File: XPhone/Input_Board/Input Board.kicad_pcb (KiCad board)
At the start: 2 copper layers, 100 x 100 mm, 94 parts, among them J1 AUDIO, J10 ENV, J11 PULSE, J12 PULSE, J13 Power In, J14 Power Out, J2 AUDIO, J3 ENV, J4 ENV, J5 PULSE, J6 PULSE, J7 AUDIO, J8 AUDIO, J9 ENV, Q1 BC847CW, Q2 BC847CW, Q3 BC847CW, Q4 BC847CW, Q5 BC847CW, Q6 BC847CW, Q7 BC847CW, Q8 BC847CW, U1 LM833, U2 78L05, U3 TL084, U4 74HC14, U5 LM833

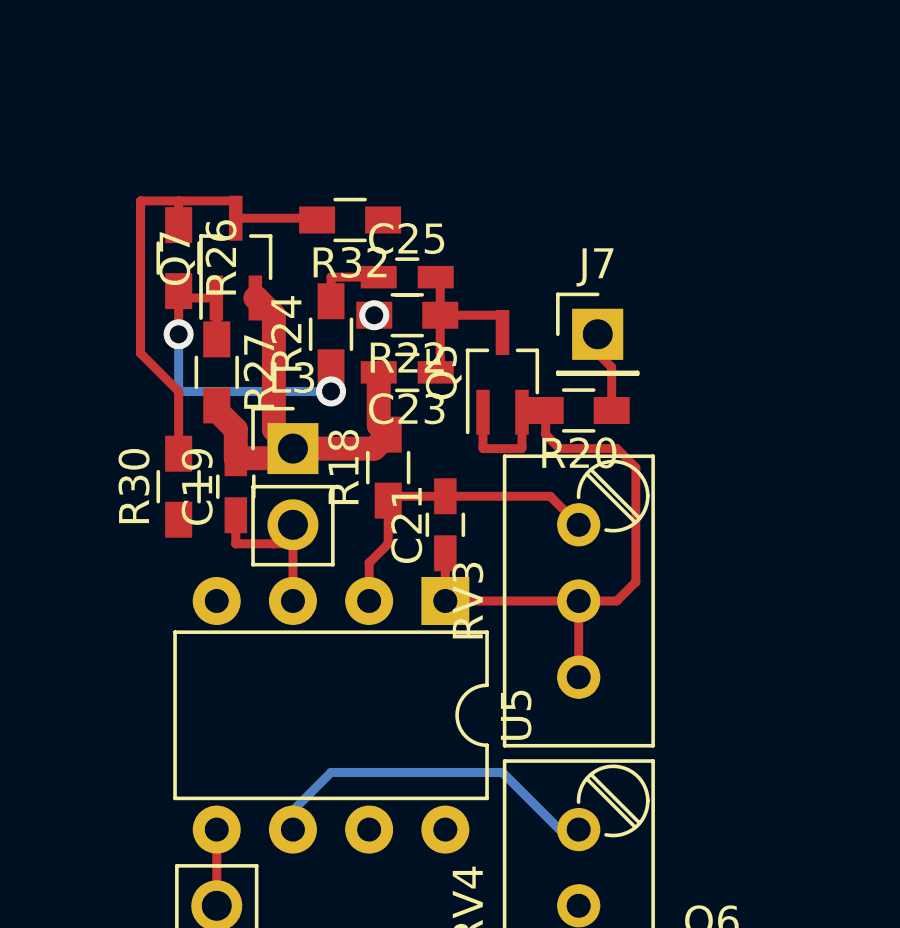
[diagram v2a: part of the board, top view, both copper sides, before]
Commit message: XPhone/Input_Board touching-up first layout of amplifier circuit
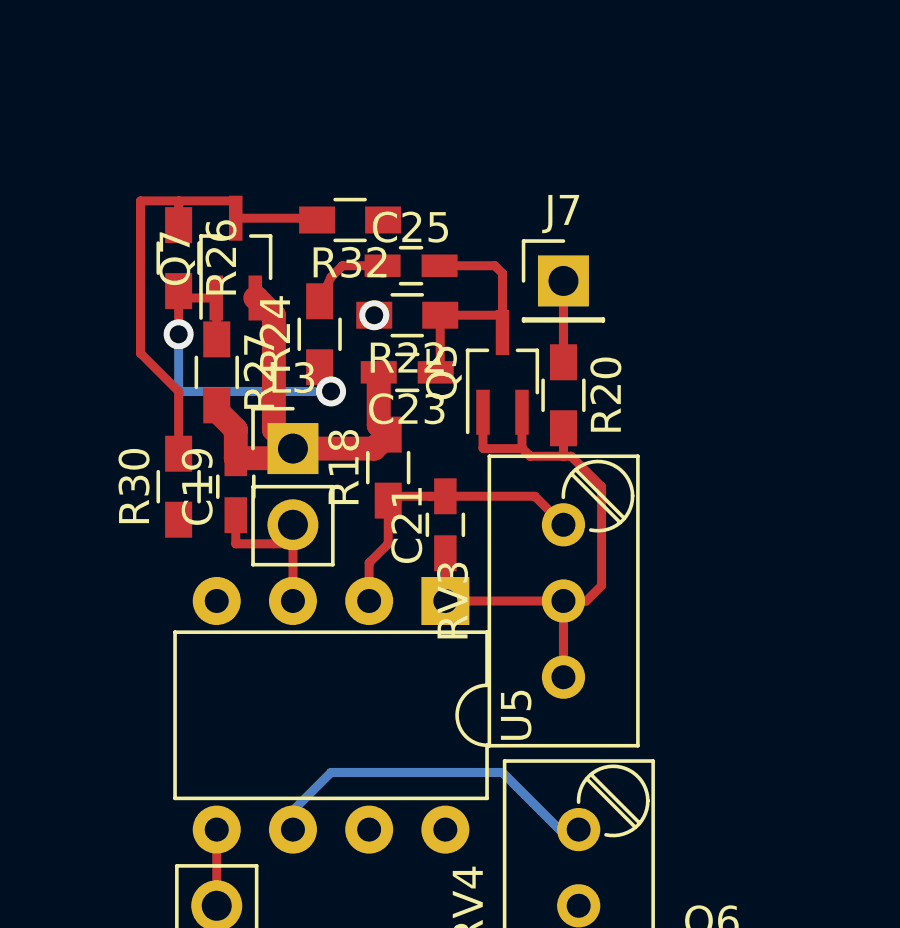
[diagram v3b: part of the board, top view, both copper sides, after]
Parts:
- moved J7 2.11 mm to (97.3, 45.2)
- moved R20 0.72 mm to (97.3, 49.0), turned to 270 degrees
- moved RV3 0.51 mm to (97.3, 53.3)
- moved C25 0.40 mm to (92.2, 44.7)
- moved R24 0.38 mm to (89.2, 47.0)
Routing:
- net Net-(C23-Pad1): track 6.03 -> 8.88 mm
- net Net-(C21-Pad1): track 23.3 -> 20.7 mm
- net Net-(C25-Pad1): track 2.40 -> 3.02 mm
- net Net-(C21-Pad2): track 10.4 -> 9.90 mm
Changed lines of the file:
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@@
   (general
     (links 173)
-    (no_connects 144)
+    (no_connects 145)
     (area 10.719999 10.719999 110.870001 110.870001)
     (thickness 1.6)
@@
   )
   (module Pin_Headers:Pin_Header_Straight_1x01_Pitch2.54mm (layer F.Cu)
-    (at 98.425 46.99)
+    (at 97.282 45.212)
     (descr "Through hole straight pin header, 1x01, 2.54mm pitch, single row")
     (tags "Through hole pin header THT 1x01 2.54mm single row")
@@
   )
   (module Potentiometers:Potentiometer_Trimmer_Bourns_3296W (layer F.Cu)
-    (at 97.79 53.34 90)
+    (at 97.282 53.34 90)
     (descr "Spindle Trimmer Potentiometer, Bourns 3296W, https://www.bourns.com/pdfs/3296.pdf")
     (tags "Spindle Trimmer Potentiometer   Bourns 3296W")
@@
   )
   (module Resistors_SMD:R_0603_HandSoldering (layer F.Cu)
-    (at 89.535 46.99 90)
+    (at 89.154 46.99 90)
     (descr "Resistor SMD 0603, hand soldering")
     (tags "resistor 0603")
@@
   )
   (module Resistors_SMD:R_0603_HandSoldering (layer F.Cu)
-    (at 97.79 49.53 180)
+    (at 97.282 49.022 270)
     (descr "Resistor SMD 0603, hand soldering")
     (tags "resistor 0603")
     (attr smd)
-    (fp_text reference R20 (at 0 -1.45 180) (layer F.SilkS)
+    (fp_text reference R20 (at 0 -1.45 270) (layer F.SilkS)
       (effects (font (size 1 1) (thickness 0.15)))
     )
-    (fp_text value 10k (at 0 1.55 180) (layer F.Fab)
+    (fp_text value 10k (at 0 1.55 270) (layer F.Fab)
       (effects (font (size 1 1) (thickness 0.15)))
     )
-    (fp_text user %R (at 0 0 180) (layer F.Fab)
+    (fp_text user %R (at 0 0 270) (layer F.Fab)
       (effects (font (size 0.5 0.5) (thickness 0.075)))
     )
@@
     (fp_line (start 1.95 0.7) (end 1.95 -0.7) (layer F.CrtYd) (width 0.05))
     (fp_line (start 1.95 0.7) (end -1.96 0.7) (layer F.CrtYd) (width 0.05))
-    (pad 1 smd rect (at -1.1 0 180) (size 1.2 0.9) (layers F.Cu F.Paste F.Mask)
+    (pad 1 smd rect (at -1.1 0 270) (size 1.2 0.9) (layers F.Cu F.Paste F.Mask)
       (net 31 "Net-(J7-Pad1)"))
-    (pad 2 smd rect (at 1.1 0 180) (size 1.2 0.9) (layers F.Cu F.Paste F.Mask)
+    (pad 2 smd rect (at 1.1 0 270) (size 1.2 0.9) (layers F.Cu F.Paste F.Mask)
       (net 17 "Net-(C21-Pad1)"))
     (model ${KISYS3DMOD}/Resistors_SMD.3dshapes/R_0603.wrl
@@
   )
   (module Capacitors_SMD:C_0603_HandSoldering (layer F.Cu)
-    (at 92.075 45.085)
+    (at 92.202 44.704)
     (descr "Capacitor SMD 0603, hand soldering")
     (tags "capacitor 0603")
@@
   (segment (start 88.265 53.975) (end 88.265 53.34) (width 0.3) (layer F.Cu) (net 15))
   (segment (start 88.265 55.88) (end 88.265 53.34) (width 0.3) (layer F.Cu) (net 15))
-  (segment (start 85.725 63.5) (end 85.725 66.04) (width 0.3) (layer F.Cu) (net 16) (status C00000))
-  (segment (start 96.69 49.53) (end 96.69 50.335) (width 0.3) (layer F.Cu) (net 17))
-  (segment (start 99.06 55.88) (end 97.79 55.88) (width 0.3) (layer F.Cu) (net 17))
-  (segment (start 99.695 55.245) (end 99.06 55.88) (width 0.3) (layer F.Cu) (net 17))
-  (segment (start 99.695 51.435) (end 99.695 55.245) (width 0.3) (layer F.Cu) (net 17))
-  (segment (start 99.06 50.8) (end 99.695 51.435) (width 0.3) (layer F.Cu) (net 17))
-  (segment (start 97.155 50.8) (end 99.06 50.8) (width 0.3) (layer F.Cu) (net 17))
-  (segment (start 96.69 50.335) (end 97.155 50.8) (width 0.3) (layer F.Cu) (net 17))
-  (segment (start 95.9 49.59) (end 96.63 49.59) (width 0.3) (layer F.Cu) (net 17))
-  (segment (start 96.63 49.59) (end 96.69 49.53) (width 0.3) (layer F.Cu) (net 17))
+  (segment (start 85.725 63.5) (end 85.725 66.04) (width 0.3) (layer F.Cu) (net 16))
+  (segment (start 97.282 50.122) (end 97.282 51.054) (width 0.3) (layer F.Cu) (net 17) (status 400000))
+  (segment (start 95.9 49.59) (end 95.9 50.785) (width 0.3) (layer F.Cu) (net 17))
+  (segment (start 95.9 50.785) (end 96.169 51.054) (width 0.3) (layer F.Cu) (net 17))
+  (segment (start 98.044 55.88) (end 97.282 55.88) (width 0.3) (layer F.Cu) (net 17))
+  (segment (start 98.552 55.372) (end 98.044 55.88) (width 0.3) (layer F.Cu) (net 17))
+  (segment (start 98.552 52.07) (end 98.552 55.372) (width 0.3) (layer F.Cu) (net 17))
+  (segment (start 97.536 51.054) (end 98.552 52.07) (width 0.3) (layer F.Cu) (net 17))
+  (segment (start 96.169 51.054) (end 97.282 51.054) (width 0.3) (layer F.Cu) (net 17))
+  (segment (start 97.282 51.054) (end 97.536 51.054) (width 0.3) (layer F.Cu) (net 17))
   (segment (start 94.6 49.59) (end 94.6 50.785) (width 0.3) (layer F.Cu) (net 17))
-  (segment (start 95.9 50.785) (end 95.9 49.59) (width 0.3) (layer F.Cu) (net 17))
   (segment (start 95.885 50.8) (end 95.9 50.785) (width 0.3) (layer F.Cu) (net 17))
   (segment (start 94.615 50.8) (end 95.885 50.8) (width 0.3) (layer F.Cu) (net 17))
   (segment (start 94.6 50.785) (end 94.615 50.8) (width 0.3) (layer F.Cu) (net 17))
   (segment (start 93.345 55.88) (end 93.345 54.29) (width 0.3) (layer F.Cu) (net 17))
-  (segment (start 97.79 55.88) (end 93.345 55.88) (width 0.3) (layer F.Cu) (net 17))
-  (segment (start 97.79 55.88) (end 97.79 58.42) (width 0.3) (layer F.Cu) (net 17))
-  (segment (start 93.345 52.39) (end 96.84 52.39) (width 0.3) (layer F.Cu) (net 18))
-  (segment (start 96.84 52.39) (end 97.79 53.34) (width 0.3) (layer F.Cu) (net 18))
-  (segment (start 93.345 52.39) (end 91.585 52.39) (width 0.3) (layer F.Cu) (net 18))
+  (segment (start 97.282 55.88) (end 93.345 55.88) (width 0.3) (layer F.Cu) (net 17) (status 10))
+  (segment (start 97.282 55.88) (end 97.282 58.42) (width 0.3) (layer F.Cu) (net 17) (status 30))
+  (segment (start 92.837 52.39) (end 96.332 52.39) (width 0.3) (layer F.Cu) (net 18))
+  (segment (start 96.332 52.39) (end 97.282 53.34) (width 0.3) (layer F.Cu) (net 18) (status 20))
+  (segment (start 92.837 52.39) (end 91.585 52.39) (width 0.3) (layer F.Cu) (net 18))
   (segment (start 91.585 52.39) (end 91.44 52.535) (width 0.3) (layer F.Cu) (net 18))
   (segment (start 90.805 55.88) (end 90.805 54.61) (width 0.3) (layer F.Cu) (net 18))
@@
   (segment (start 89.535 61.595) (end 88.265 62.865) (width 0.3) (layer B.Cu) (net 20))
   (segment (start 88.265 62.865) (end 88.265 63.5) (width 0.3) (layer B.Cu) (net 20))
-  (segment (start 93.175 46.355) (end 93.175 45.235) (width 0.3) (layer F.Cu) (net 21))
-  (segment (start 93.175 45.235) (end 93.025 45.085) (width 0.3) (layer F.Cu) (net 21))
+  (segment (start 93.152 44.704) (end 94.996 44.704) (width 0.3) (layer F.Cu) (net 21))
+  (segment (start 95.25 44.958) (end 95.25 46.93) (width 0.3) (layer F.Cu) (net 21))
+  (segment (start 94.996 44.704) (end 95.25 44.958) (width 0.3) (layer F.Cu) (net 21))
   (segment (start 93.175 46.355) (end 95.25 46.355) (width 0.3) (layer F.Cu) (net 21))
   (segment (start 95.25 46.355) (end 95.25 46.93) (width 0.3) (layer F.Cu) (net 21))
@@
   (segment (start 93.175 48.11) (end 93.025 48.26) (width 0.3) (layer F.Cu) (net 21))
   (segment (start 93.235 46.295) (end 93.175 46.355) (width 0.3) (layer F.Cu) (net 21) (status 30))
-  (segment (start 91.125 45.085) (end 89.535 45.085) (width 0.3) (layer F.Cu) (net 23))
-  (segment (start 89.535 45.085) (end 89.535 45.89) (width 0.3) (layer F.Cu) (net 23))
-  (segment (start 98.425 46.99) (end 98.425 47.625) (width 0.3) (layer F.Cu) (net 31))
-  (segment (start 98.425 47.625) (end 98.89 48.09) (width 0.3) (layer F.Cu) (net 31))
-  (segment (start 98.89 48.09) (end 98.89 49.53) (width 0.3) (layer F.Cu) (net 31))
+  (segment (start 91.252 44.704) (end 89.916 44.704) (width 0.3) (layer F.Cu) (net 23))
+  (segment (start 89.535 45.085) (end 89.154 45.89) (width 0.3) (layer F.Cu) (net 23) (status 20))
+  (segment (start 89.916 44.704) (end 89.535 45.085) (width 0.3) (layer F.Cu) (net 23))
+  (segment (start 91.252 44.704) (end 91.252 44.958) (width 0.3) (layer F.Cu) (net 23))
+  (segment (start 97.282 47.922) (end 97.282 45.212) (width 0.3) (layer F.Cu) (net 31) (status C00000))
   (via (at 90.975 46.355) (size 1) (drill 0.6) (layers F.Cu B.Cu) (net 37))
   (segment (start 90.975 46.355) (end 90.805 46.355) (width 0.3) (layer B.Cu) (net 37))
@@
   (segment (start 85.725 47.16) (end 85.725 45.795) (width 0.3) (layer F.Cu) (net 44))
   (segment (start 85.725 45.795) (end 85.71 45.78) (width 0.3) (layer F.Cu) (net 44))
-  (segment (start 89.535 48.09) (end 89.535 48.895) (width 0.3) (layer F.Cu) (net 44) (status 10))
+  (segment (start 89.154 48.09) (end 89.535 48.895) (width 0.3) (layer F.Cu) (net 44) (status 10))
   (segment (start 84.455 46.99) (end 84.455 45.55) (width 0.3) (layer F.Cu) (net 44))
   (via (at 84.455 46.99) (size 1) (drill 0.6) (layers F.Cu B.Cu) (net 44))

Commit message: XPhone/Input_Board
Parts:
- moved J13 102.2 mm to (43.7, 211.1)
- moved J14 102.2 mm to (43.7, 208.5)
- moved C10 101.9 mm to (14.1, 211.1)
- moved C11 101.9 mm to (18.5, 211.1)
- moved C12 101.9 mm to (23.0, 211.1)
- moved C15 101.9 mm to (33.5, 134.7)
- moved C17 101.9 mm to (27.4, 211.1)
- moved C3 101.9 mm to (24.1, 144.9)
- moved C4 101.9 mm to (25.5, 173.6)
- moved C7 101.9 mm to (24.4, 150.9)
- moved C8 101.9 mm to (37.6, 177.4)
- moved J1 101.9 mm to (22.2, 137.7)
- moved J11 101.9 mm to (97.3, 122.2)
- moved J6 101.9 mm to (30.0, 197.1)
- moved L1 101.9 mm to (31.1, 149.0)
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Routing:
- net Net-(Q7-Pad3): track 16.2 -> 4.45 mm
- net Net-(C21-Pad2): track 9.90 -> 10.4 mm
